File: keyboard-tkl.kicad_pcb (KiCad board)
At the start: 2 copper layers, 108 parts, among them P1 USB_OTG, P2 JTAG, U1 AT32UC3B1512, U2 74HC595, U3 74HC595, U4 74HC595, U5 LD1117S33CTR, Y1 12MHz

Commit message: lots of pcb work
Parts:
- Cjtag1, Cout1, Cout2, Cx1, Cx2, P1, P2, R1, R2, R3, R4, R5, R6, R7, R8, U1, U2, U3, U4, U5: moved to B.Cu
- moved SW-PGUP1 531.5 mm to (394.0, 129.0)
- moved SW-DOWN1 516.2 mm to (375.0, 205.0)
- moved SW-HOME1 498.2 mm to (375.0, 129.0)
- moved SW-RIGHT1 495.6 mm to (394.0, 205.0)
- moved SW-SHIFT2 488.5 mm to (315.4, 186.0)
- moved SW-CTRL2 488.2 mm to (329.6, 205.0)
- moved SW-LEFT1 484.9 mm to (356.0, 205.0)
- moved SW-MENU1 466.1 mm to (305.9, 205.0)
- moved SW-END1 462.7 mm to (374.9, 148.0)
- moved SW-PRINT1 428.0 mm to (356.0, 105.0)
- moved SW-]1 416.8 mm to (303.5, 148.0)
- moved SW-DEL1 408.6 mm to (356.0, 148.0)
- moved SW-PAUSE1 406.3 mm to (394.0, 105.0)
- moved SW-F10 401.8 mm to (294.0, 105.0)
- moved SW-PG-DWN1 400.3 mm to (394.0, 148.0)
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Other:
- board outline added: 360 x 130 mm
- copper layers 2 -> 4

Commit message: pcb layout updates
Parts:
- P2: moved to F.Cu
- moved P2 71.0 mm to (376.5, 117.5)
- moved Cx1 65.2 mm to (339.0, 104.0), turned to 0 degrees
- moved Y1 63.8 mm to (345.0, 107.1)
- moved Cjtag1 63.2 mm to (381.0, 111.0)
- moved Cout1 63.2 mm to (362.6, 104.1)
- moved Cout2 63.2 mm to (362.6, 110.1)
- moved P1 63.2 mm to (323.0, 35.4)
- moved R1 63.2 mm to (321.6, 101.1)
- moved R2 63.2 mm to (321.6, 107.1)
- moved R3 63.2 mm to (321.6, 113.1)
- moved R4 63.2 mm to (321.6, 119.1)
- moved R5 63.2 mm to (321.6, 125.1)
- moved R6 63.2 mm to (321.6, 131.1)
- moved R7 63.2 mm to (321.6, 137.1)
- moved R8 63.2 mm to (321.6, 143.1)
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
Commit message: Add stabs to big keys
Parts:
- added SW1: MX, mx1a:MXST, F.Cu at (115.6, 144.8)
- added SW2: MX, mx1a:MXST, F.Cu at (219.7, 144.8)
- added SW3: MX, mx1a:MXST, F.Cu at (279.4, 124.5)
- added SW4: MX, mx1a:MXST, F.Cu at (311.1, 124.5)
- added SW5: MX, mx1a:MXST, F.Cu at (43.2, 124.5)
- added SW6: MX, mx1a:MXST, F.Cu at (72.4, 124.5)
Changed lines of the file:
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@@
-(kicad_pcb (version 4) (host pcbnew "(2015-08-16 BZR 6097, Git b384c94)-product")
+(kicad_pcb (version 4) (host pcbnew "(2015-08-01 BZR 6034)-product")
   (general
     (links 253)
     (no_connects 253)
-    (area 49.924999 89.924999 410.075001 220.075001)
+    (area 29.924999 29.924999 390.075001 160.075001)
     (thickness 1.6)
     (drawings 8)
     (tracks 0)
     (zones 0)
-    (modules 108)
-    (nets 68)
+    (modules 114)
+    (nets 80)
   )
   (page A3)
@@
   (net 66 "Net-(U1-Pad44)")
   (net 67 "Net-(U1-Pad46)")
+  (net 68 "Net-(SW1-Pad1)")
+  (net 69 "Net-(SW1-Pad2)")
+  (net 70 "Net-(SW2-Pad1)")
+  (net 71 "Net-(SW2-Pad2)")
+  (net 72 "Net-(SW3-Pad1)")
+  (net 73 "Net-(SW3-Pad2)")
+  (net 74 "Net-(SW4-Pad1)")
+  (net 75 "Net-(SW4-Pad2)")
+  (net 76 "Net-(SW5-Pad1)")
+  (net 77 "Net-(SW5-Pad2)")
+  (net 78 "Net-(SW6-Pad1)")
+  (net 79 "Net-(SW6-Pad2)")
   (net_class Default "This is the default net class."
     (clearance 0.2)
@@
     (add_net "Net-(R1-Pad2)")
     (add_net "Net-(R2-Pad2)")
+    (add_net "Net-(SW1-Pad1)")
+    (add_net "Net-(SW1-Pad2)")
+    (add_net "Net-(SW2-Pad1)")
+    (add_net "Net-(SW2-Pad2)")
+    (add_net "Net-(SW3-Pad1)")
+    (add_net "Net-(SW3-Pad2)")
+    (add_net "Net-(SW4-Pad1)")
+    (add_net "Net-(SW4-Pad2)")
+    (add_net "Net-(SW5-Pad1)")
+    (add_net "Net-(SW5-Pad2)")
+    (add_net "Net-(SW6-Pad1)")
+    (add_net "Net-(SW6-Pad2)")
     (add_net "Net-(U1-Pad20)")
     (add_net "Net-(U1-Pad21)")
@@
       (net 1 +3V3))
   )
+  (module mx1a:MXST (layer F.Cu)
+    (at 115.57 144.78)
+    (fp_text reference SW1 (at 2.54 -6.35 90) (layer F.SilkS) hide
+      (effects (font (size 0.5 0.5) (thickness 0.1)))
+    )
+    (fp_text value MX (at -2.54 8.89 90) (layer F.SilkS)
+      (effects (font (size 0.5 0.5) (thickness 0.1)))
+    )
+    (fp_line (start 3.429 10.668) (end 3.429 -8.001) (layer F.SilkS) (width 0.381))
+    (fp_line (start 3.429 -8.001) (end -3.429 -8.001) (layer F.SilkS) (width 0.381))
+    (fp_line (start -3.429 -8.001) (end -3.429 10.668) (layer F.SilkS) (width 0.381))
+    (fp_line (start -3.429 10.668) (end 3.429 10.668) (layer F.SilkS) (width 0.381))
+    (pad 1 thru_hole circle (at 0 -6.985) (size 3.048 3.048) (drill 3.048) (layers *.Cu *.Mask F.SilkS)
+      (net 68 "Net-(SW1-Pad1)"))
+    (pad 2 thru_hole circle (at 0 8.255) (size 3.9802 3.9802) (drill 3.9802) (layers *.Cu *.Mask F.SilkS)
+      (net 69 "Net-(SW1-Pad2)"))
+    (model cherry_mx1.wrl
+      (at (xyz 0 0 0))
+      (scale (xyz 1 1 1))
+      (rotate (xyz 0 0 0))
+    )
+  )
+  (module mx1a:MXST (layer F.Cu)
+    (at 219.71 144.78)
+    (fp_text reference SW2 (at 2.54 -6.35 90) (layer F.SilkS) hide
+      (effects (font (size 0.5 0.5) (thickness 0.1)))
+    )
+    (fp_text value MX (at -2.54 8.89 90) (layer F.SilkS)
+      (effects (font (size 0.5 0.5) (thickness 0.1)))
+    )
+    (fp_line (start 3.429 10.668) (end 3.429 -8.001) (layer F.SilkS) (width 0.381))
+    (fp_line (start 3.429 -8.001) (end -3.429 -8.001) (layer F.SilkS) (width 0.381))
+    (fp_line (start -3.429 -8.001) (end -3.429 10.668) (layer F.SilkS) (width 0.381))
+    (fp_line (start -3.429 10.668) (end 3.429 10.668) (layer F.SilkS) (width 0.381))
+    (pad 1 thru_hole circle (at 0 -6.985) (size 3.048 3.048) (drill 3.048) (layers *.Cu *.Mask F.SilkS)
+      (net 70 "Net-(SW2-Pad1)"))
+    (pad 2 thru_hole circle (at 0 8.255) (size 3.9802 3.9802) (drill 3.9802) (layers *.Cu *.Mask F.SilkS)
+      (net 71 "Net-(SW2-Pad2)"))
+    (model cherry_mx1.wrl
+      (at (xyz 0 0 0))
+      (scale (xyz 1 1 1))
+      (rotate (xyz 0 0 0))
+    )
+  )
+  (module mx1a:MXST (layer F.Cu)
+    (at 279.4 124.46)
+    (fp_text reference SW3 (at 2.54 -6.35 90) (layer F.SilkS) hide
+      (effects (font (size 0.5 0.5) (thickness 0.1)))
+    )
+    (fp_text value MX (at -2.54 8.89 90) (layer F.SilkS)
+      (effects (font (size 0.5 0.5) (thickness 0.1)))
+    )
+    (fp_line (start 3.429 10.668) (end 3.429 -8.001) (layer F.SilkS) (width 0.381))
+    (fp_line (start 3.429 -8.001) (end -3.429 -8.001) (layer F.SilkS) (width 0.381))
+    (fp_line (start -3.429 -8.001) (end -3.429 10.668) (layer F.SilkS) (width 0.381))
+    (fp_line (start -3.429 10.668) (end 3.429 10.668) (layer F.SilkS) (width 0.381))
+    (pad 1 thru_hole circle (at 0 -6.985) (size 3.048 3.048) (drill 3.048) (layers *.Cu *.Mask F.SilkS)
+      (net 72 "Net-(SW3-Pad1)"))
+    (pad 2 thru_hole circle (at 0 8.255) (size 3.9802 3.9802) (drill 3.9802) (layers *.Cu *.Mask F.SilkS)
+      (net 73 "Net-(SW3-Pad2)"))
+    (model cherry_mx1.wrl
+      (at (xyz 0 0 0))
+      (scale (xyz 1 1 1))
+      (rotate (xyz 0 0 0))
+    )
+  )
+  (module mx1a:MXST (layer F.Cu)
+    (at 311.15 124.46)
+    (fp_text reference SW4 (at 2.54 -6.35 90) (layer F.SilkS) hide
+      (effects (font (size 0.5 0.5) (thickness 0.1)))
+    )
+    (fp_text value MX (at -2.54 8.89 90) (layer F.SilkS)
+      (effects (font (size 0.5 0.5) (thickness 0.1)))
+    )
+    (fp_line (start 3.429 10.668) (end 3.429 -8.001) (layer F.SilkS) (width 0.381))
+    (fp_line (start 3.429 -8.001) (end -3.429 -8.001) (layer F.SilkS) (width 0.381))
+    (fp_line (start -3.429 -8.001) (end -3.429 10.668) (layer F.SilkS) (width 0.381))
+    (fp_line (start -3.429 10.668) (end 3.429 10.668) (layer F.SilkS) (width 0.381))
+    (pad 1 thru_hole circle (at 0 -6.985) (size 3.048 3.048) (drill 3.048) (layers *.Cu *.Mask F.SilkS)
+      (net 74 "Net-(SW4-Pad1)"))
+    (pad 2 thru_hole circle (at 0 8.255) (size 3.9802 3.9802) (drill 3.9802) (layers *.Cu *.Mask F.SilkS)
+      (net 75 "Net-(SW4-Pad2)"))
+    (model cherry_mx1.wrl
+      (at (xyz 0 0 0))
+      (scale (xyz 1 1 1))
+      (rotate (xyz 0 0 0))
+    )
+  )
+  (module mx1a:MXST (layer F.Cu)
+    (at 43.18 124.46)
+    (fp_text reference SW5 (at 2.54 -6.35 90) (layer F.SilkS) hide
+      (effects (font (size 0.5 0.5) (thickness 0.1)))
+    )
+    (fp_text value MX (at -2.54 8.89 90) (layer F.SilkS)
+      (effects (font (size 0.5 0.5) (thickness 0.1)))
+    )
+    (fp_line (start 3.429 10.668) (end 3.429 -8.001) (layer F.SilkS) (width 0.381))
+    (fp_line (start 3.429 -8.001) (end -3.429 -8.001) (layer F.SilkS) (width 0.381))
+    (fp_line (start -3.429 -8.001) (end -3.429 10.668) (layer F.SilkS) (width 0.381))
+    (fp_line (start -3.429 10.668) (end 3.429 10.668) (layer F.SilkS) (width 0.381))
+    (pad 1 thru_hole circle (at 0 -6.985) (size 3.048 3.048) (drill 3.048) (layers *.Cu *.Mask F.SilkS)
+      (net 76 "Net-(SW5-Pad1)"))
+    (pad 2 thru_hole circle (at 0 8.255) (size 3.9802 3.9802) (drill 3.9802) (layers *.Cu *.Mask F.SilkS)
+      (net 77 "Net-(SW5-Pad2)"))
+    (model cherry_mx1.wrl
+      (at (xyz 0 0 0))
+      (scale (xyz 1 1 1))
+      (rotate (xyz 0 0 0))
+    )
+  )
+  (module mx1a:MXST (layer F.Cu)
+    (at 72.39 124.46)
+    (fp_text reference SW6 (at 2.54 -6.35 90) (layer F.SilkS) hide
+      (effects (font (size 0.5 0.5) (thickness 0.1)))
+    )
+    (fp_text value MX (at -2.54 8.89 90) (layer F.SilkS)
+      (effects (font (size 0.5 0.5) (thickness 0.1)))
+    )
+    (fp_line (start 3.429 10.668) (end 3.429 -8.001) (layer F.SilkS) (width 0.381))
+    (fp_line (start 3.429 -8.001) (end -3.429 -8.001) (layer F.SilkS) (width 0.381))
+    (fp_line (start -3.429 -8.001) (end -3.429 10.668) (layer F.SilkS) (width 0.381))
+    (fp_line (start -3.429 10.668) (end 3.429 10.668) (layer F.SilkS) (width 0.381))
+    (pad 1 thru_hole circle (at 0 -6.985) (size 3.048 3.048) (drill 3.048) (layers *.Cu *.Mask F.SilkS)
+      (net 78 "Net-(SW6-Pad1)"))
+    (pad 2 thru_hole circle (at 0 8.255) (size 3.9802 3.9802) (drill 3.9802) (layers *.Cu *.Mask F.SilkS)
+      (net 79 "Net-(SW6-Pad2)"))
+    (model cherry_mx1.wrl
+      (at (xyz 0 0 0))
+      (scale (xyz 1 1 1))
+      (rotate (xyz 0 0 0))
+    )
+  )
   (gr_arc (start 35 155) (end 35 160) (angle 90) (layer Edge.Cuts) (width 0.15))

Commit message: Stabilizers placed and spaced
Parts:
- added SW7: MX, mx1a:MXST, F.Cu at (312.1, 107.0)
- added SW8: MX, mx1a:MXST, F.Cu at (288.1, 107.0)
- moved SW3 4.26 mm to (283.4, 126.0)
- moved SW4 4.08 mm to (307.4, 126.0)
- moved SW5 2.70 mm to (45.9, 124.5)
- moved SW2 2.59 mm to (217.1, 145.0)
- moved SW6 2.52 mm to (69.9, 124.5)
- moved SW1 1.57 mm to (117.1, 145.0)
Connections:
- net +3V3 renamed VCC

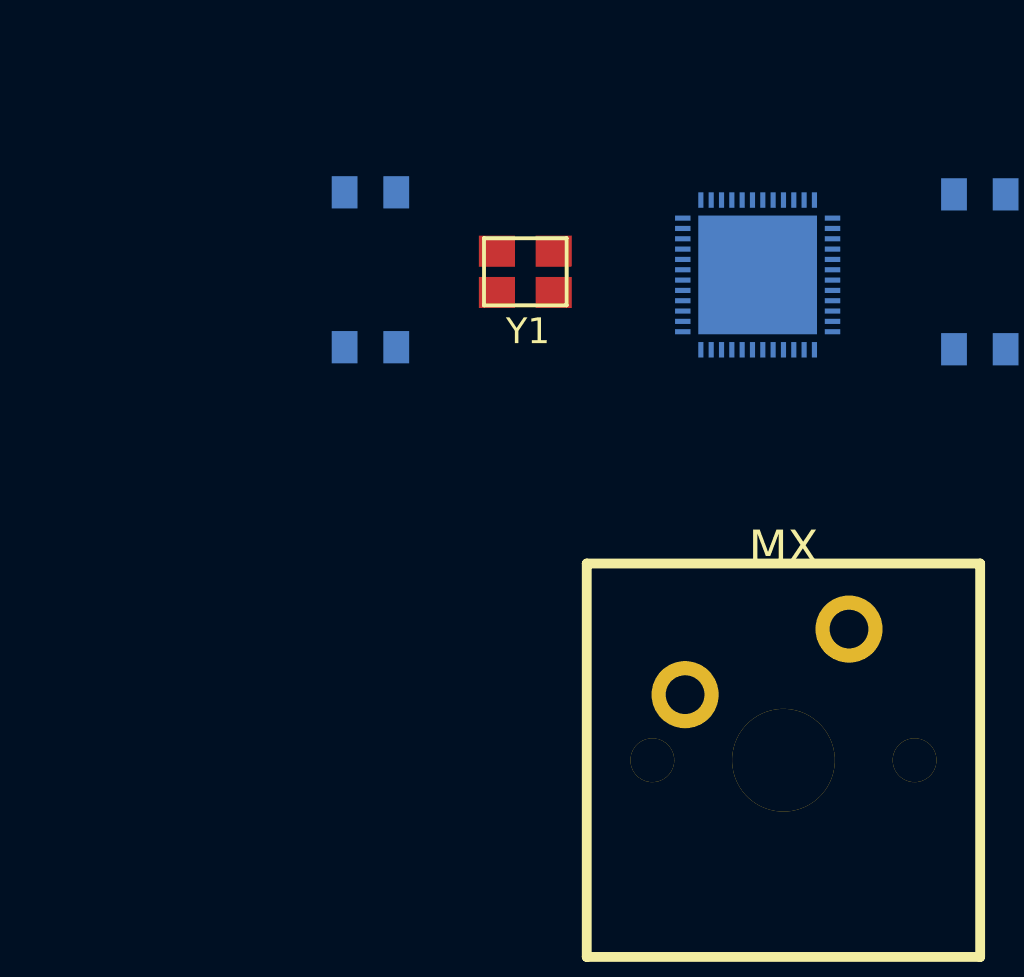
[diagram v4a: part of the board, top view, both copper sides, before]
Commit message: LEDs added, but not placed
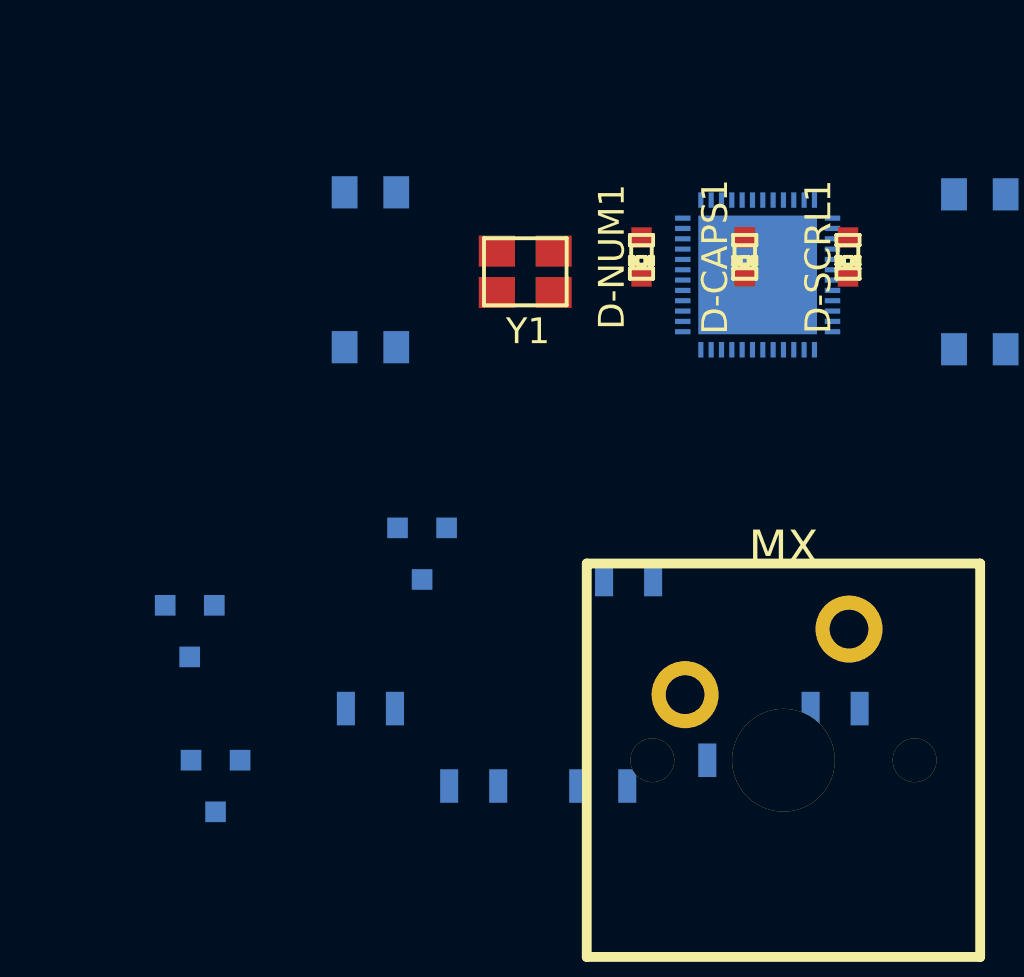
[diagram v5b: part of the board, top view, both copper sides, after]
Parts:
- added D-CAPS1: LED, LEDs:LED-0603, F.Cu at (353.5, 106.5)
- added D-NUM1: LED, LEDs:LED-0603, F.Cu at (349.5, 106.5)
- added D-SCRL1: LED, LEDs:LED-0603, F.Cu at (357.5, 106.5)
- added Q1: Q_NMOS_GSD, Housings_SOT-23_SOT-143_TSOT-6:SOT-23, B.Cu at (333.0, 127.0)
- added Q2: Q_NMOS_GSD, Housings_SOT-23_SOT-143_TSOT-6:SOT-23, B.Cu at (332.0, 121.0)
- added Q3: Q_NMOS_GSD, Housings_SOT-23_SOT-143_TSOT-6:SOT-23, B.Cu at (341.0, 118.0)
- added R10: 400, Resistors_SMD:R_0805, B.Cu at (343.0, 127.0)
- added R11: 10K, Resistors_SMD:R_0805, B.Cu at (353.0, 126.0)
- added R12: 400, Resistors_SMD:R_0805, B.Cu at (357.0, 124.0)
- added R13: 10K, Resistors_SMD:R_0805, B.Cu at (349.0, 119.0)
- added R14: 400, Resistors_SMD:R_0805, B.Cu at (339.0, 124.0)
- added R9: 10k, Resistors_SMD:R_0805, B.Cu at (348.0, 127.0)
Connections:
- U1 pad 25: Net-(U1-Pad25) -> /CAPS
- U1 pad 26: Net-(U1-Pad26) -> /SCRL
- U1 pad 27: Net-(U1-Pad27) -> /NUM
